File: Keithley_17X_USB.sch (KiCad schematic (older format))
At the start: 42 parts, among them J1 USB_B, J2 SIGNAL INPUT, J3 PROG, U1 TLP281-4, U2 TLP281-4, U3 MIC5504-3.3YM5, U4 MSP430FR2110, U5 FT230XS

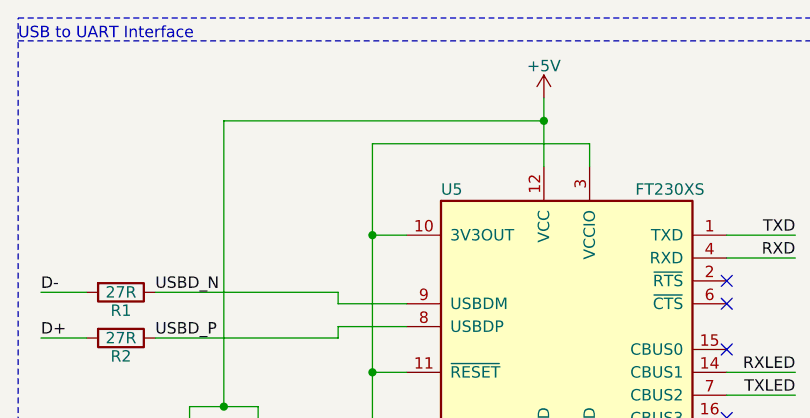
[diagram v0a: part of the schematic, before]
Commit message: label VCCIO net
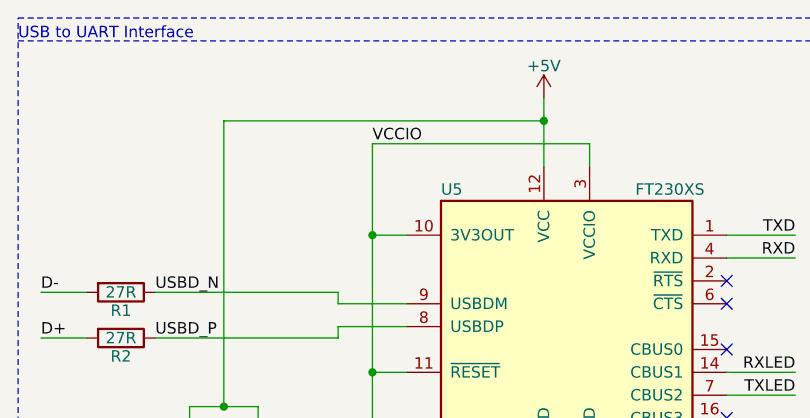
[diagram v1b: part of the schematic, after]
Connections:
- net VCCIO: now reaches C7.1, U5.10 (3V3OUT), U5.11 (~RESET), U5.3 (VCCIO)
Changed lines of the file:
@@
 	1    0    0    -1
 $EndComp
+Text Label 8500 1100 0    50   ~ 0
+VCCIO
 $EndSCHEMATC

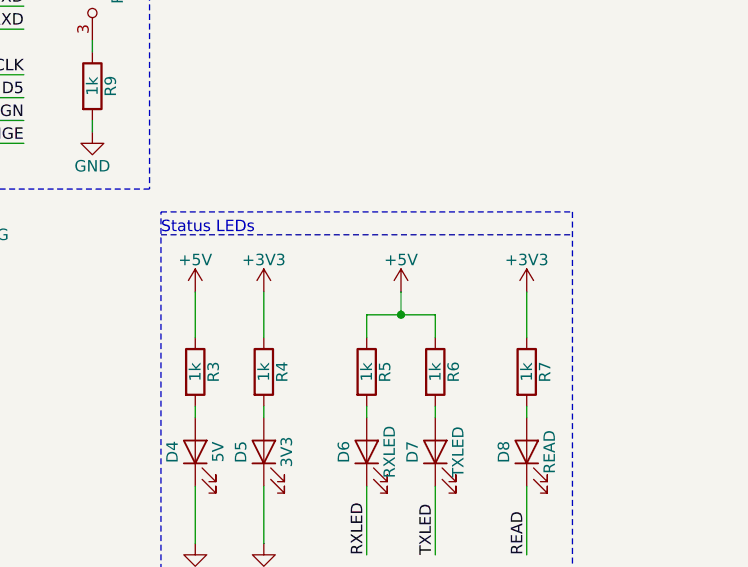
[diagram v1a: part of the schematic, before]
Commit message: rx/tx leds powered using vccio
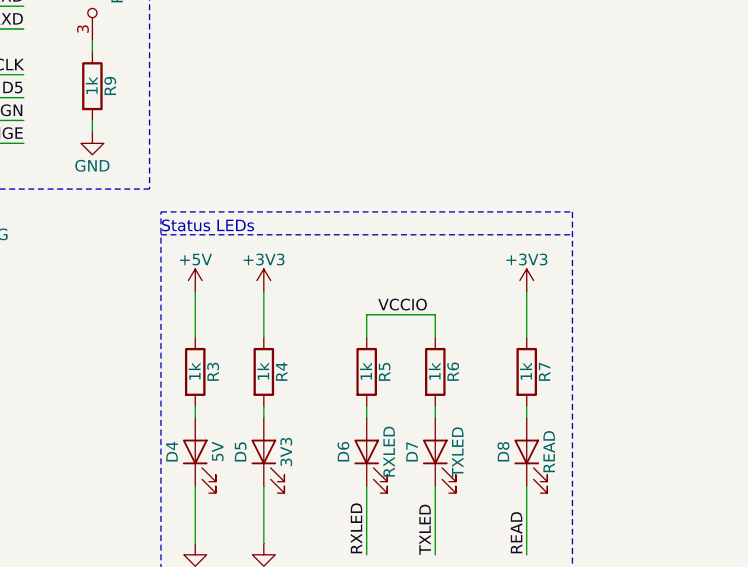
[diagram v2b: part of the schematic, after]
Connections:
- net +5V: no longer R5.1, R6.1
- net VCCIO: now also R5.1, R6.1
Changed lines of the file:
@@
 $EndComp
-Wire Wire Line
-	9550 5500 9700 5500
 Wire Wire Line
 	9850 5500 9850 5600
@@
 Connection ~ 5500 3550
 $Comp
-L power:+5V #PWR027
-U 1 1 5C687537
-P 9700 5400
-F 0 "#PWR027" H 9700 5250 50  0001 C CNN
-F 1 "+5V" H 9700 5540 50  0000 C CNN
-F 2 "" H 9700 5400 50  0001 C CNN
-F 3 "" H 9700 5400 50  0001 C CNN
-	1    9700 5400
-	1    0    0    -1
-$EndComp
-Wire Wire Line
-	9700 5400 9700 5500
-Connection ~ 9700 5500
-Wire Wire Line
-	9700 5500 9850 5500
-$Comp
 L power:+5V #PWR07
 U 1 1 5C6E6A45
@@
 Text Label 8500 1100 0    50   ~ 0
 VCCIO
+Wire Wire Line
+	9550 5500 9850 5500
+Text Label 9600 5500 0    50   ~ 0
+VCCIO
 $EndSCHEMATC
